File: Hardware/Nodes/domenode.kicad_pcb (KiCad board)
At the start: 2 copper layers, 100 x 70 mm, 86 parts, among them J1 MIC_JUMPER, J10 5V, J11 TOUCH, J12 24V, J13 CAN_BOARD, J15 RGB_SHIELD, J16 RGB_SHIELD, J17 GROVE/I2C, J18 ISP, J19 CAN_IN, J2 MIC_HEADER, J20 CAN_OUT, J21 SWITCHES, J3 SW0, J4 CANTERM, J5 3V3, J6 POWER_TEST, J9 SENSOR, Q1 MMBT918 (2N706 equiv), Q2 MMBT2222A (2N2222 equiv), SW1 SW1, SW2 SW2, SW3 RESET, SW4 BOOT, U1 MINI-360, U2 AMS1117-3.3, U3 ESP32-WROOM, U5 TSDP341xx, U6 SN65HVD230

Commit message: woooo
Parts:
- moved SW1 1.27 mm to (159.8, 136.5)
- moved SW2 1.25 mm to (165.9, 136.5)
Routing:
- net CANGND: track 84.3 -> 113.9 mm, vias 4 -> 6
- net SW1: track 32.4 -> 17.9 mm
- net SW2: track 31.0 -> 29.3 mm

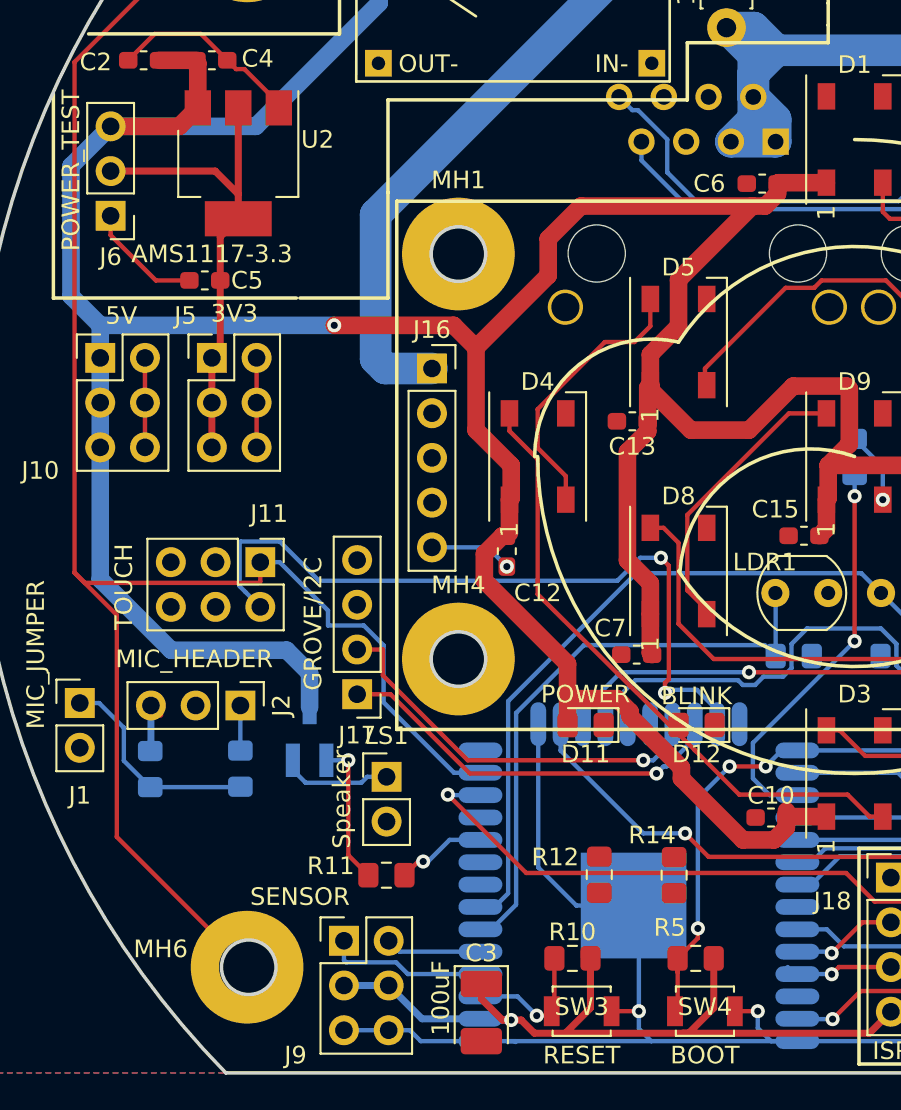
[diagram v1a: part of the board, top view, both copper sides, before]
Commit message: Added moar decoupling caps and laid out in PCB
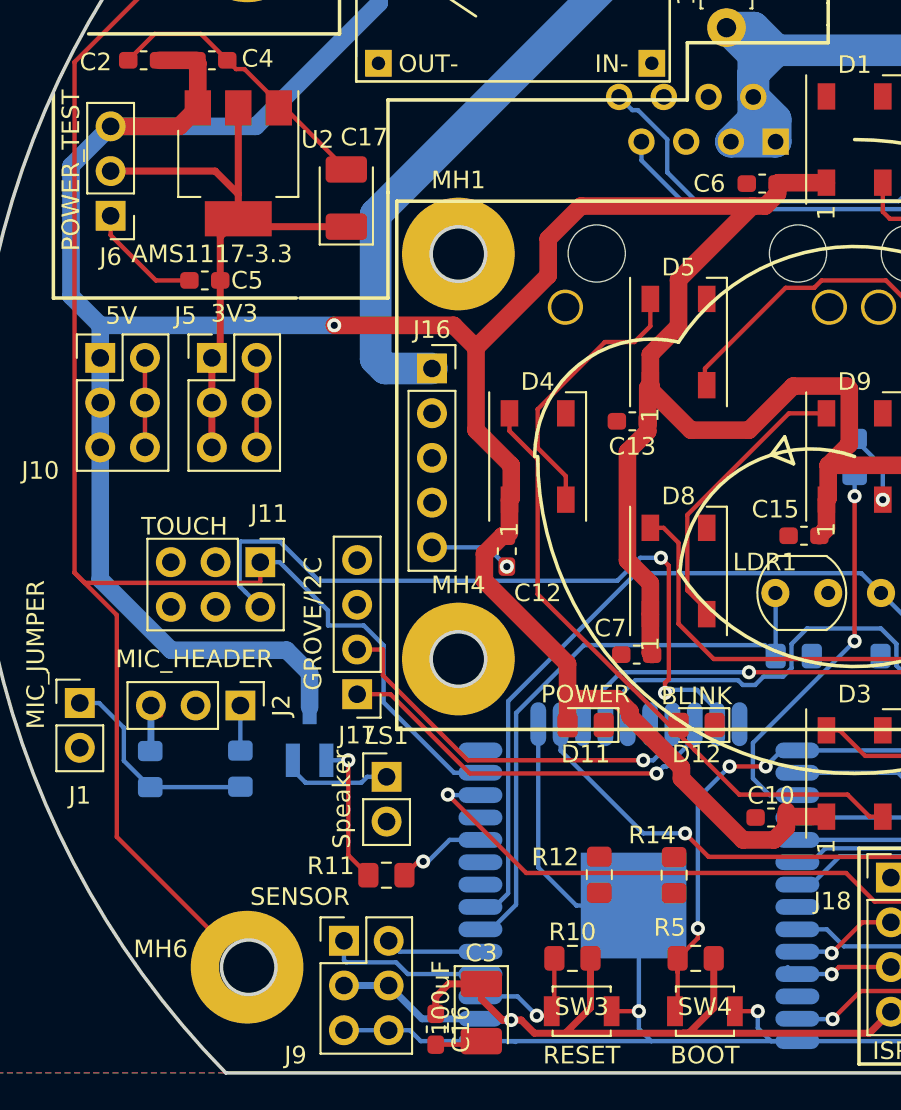
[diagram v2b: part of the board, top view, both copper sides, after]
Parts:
- added C16: 10uF, Capacitor_SMD:C_0603_1608Metric_Pad1.05x0.95mm_HandSolder, F.Cu at (124.7, 137.5)
- added C17: 100uF, Capacitor_Tantalum_SMD:CP_EIA-3528-21_Kemet-B_Pad1.50x2.35mm_HandSolder, F.Cu at (119.6, 90.3)
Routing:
- net VCC: track 95.6 -> 105.8 mm
- net CANGND: track 113.9 -> 121.9 mm

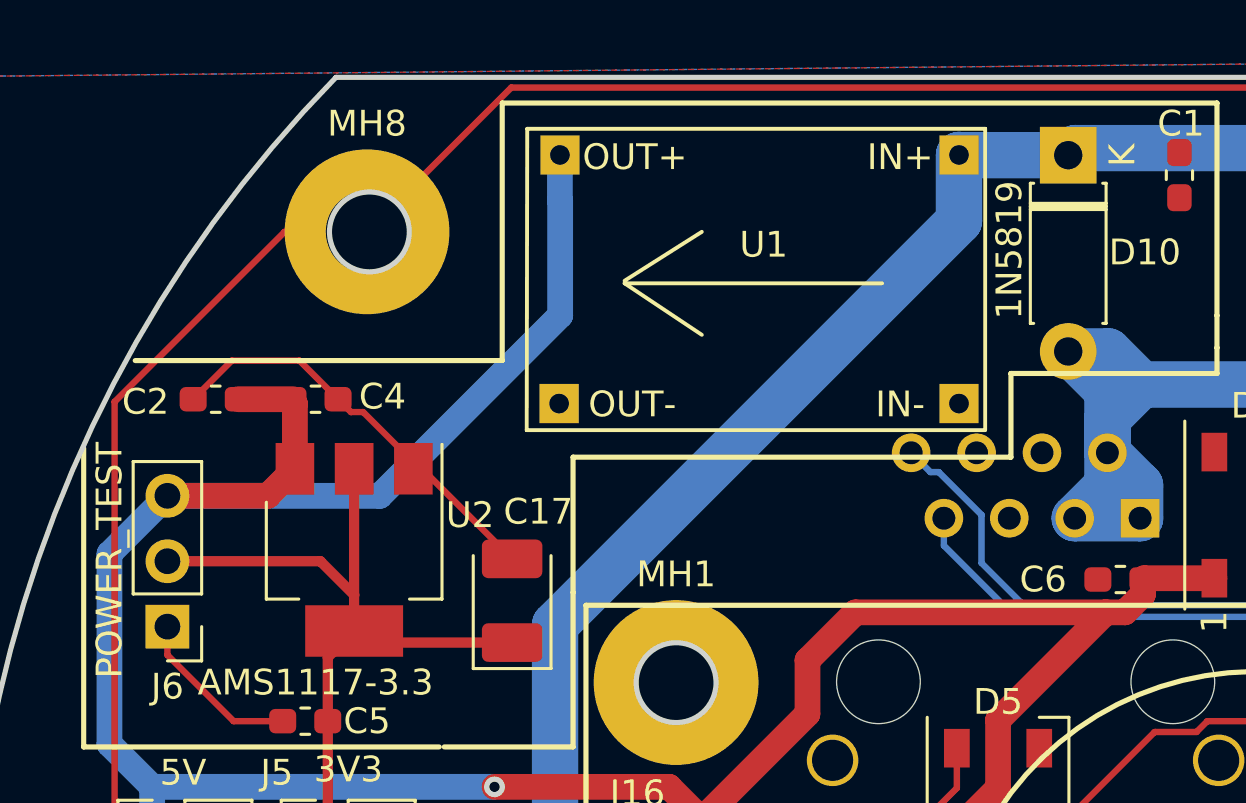
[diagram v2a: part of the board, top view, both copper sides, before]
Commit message: Updated buck regulator footprint to make it easier to solder
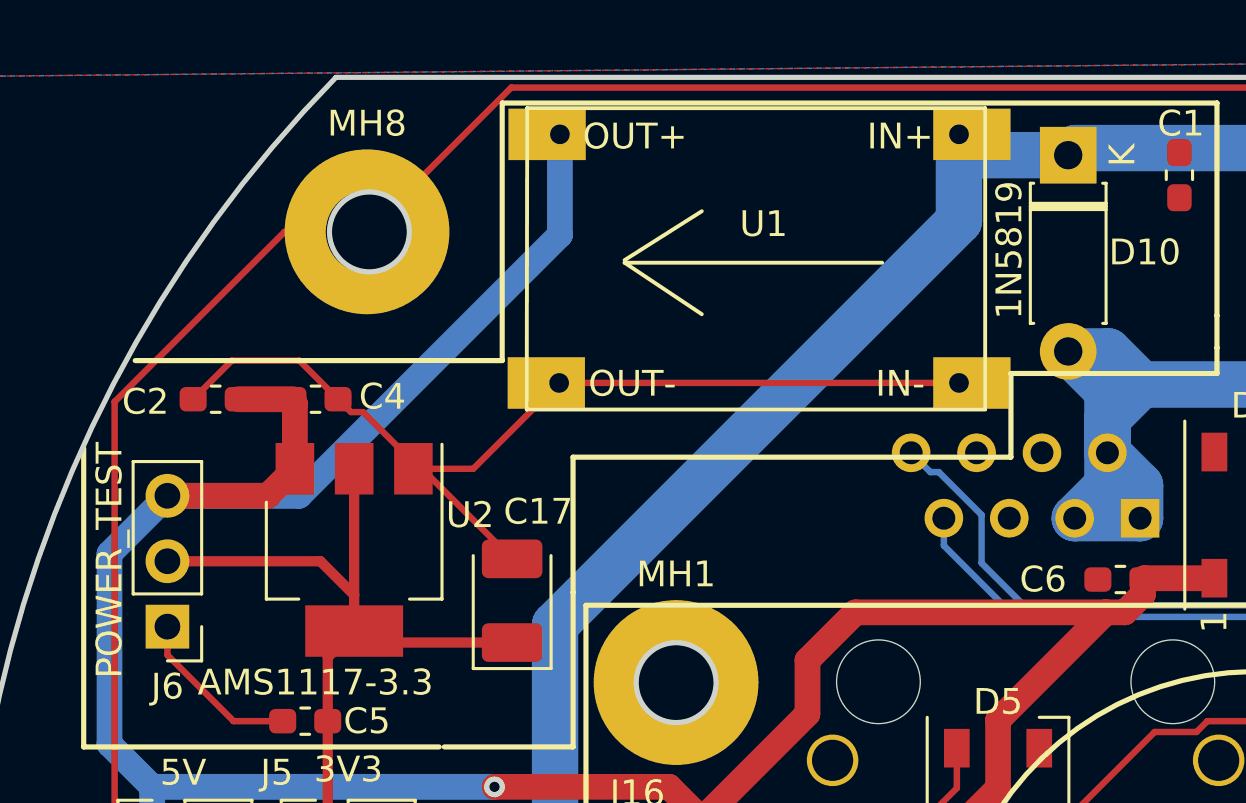
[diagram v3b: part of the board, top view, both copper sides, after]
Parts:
- moved U1 0.80 mm to (138.0, 71.2)
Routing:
- net CANGND: track 121.9 -> 144.4 mm
- net +24V: track 101.8 -> 102.9 mm
- net +5V: track 273.8 -> 272.7 mm

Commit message: Skookum'd C1
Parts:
- C1: footprint Capacitor_SMD:C_0603_1608Metric_Pad1.05x0.95mm_HandSolder -> Capacitor_SMD:C_1210_3225Metric_Pad1.42x2.65mm_HandSolder
- moved D12 7.20 mm to (134.6, 125.5), turned to 270 degrees
- moved D11 6.57 mm to (137.2, 125.5), turned to 90 degrees
- moved R14 3.69 mm to (134.6, 129.3)
- moved R12 3.27 mm to (137.2, 129.4)
- moved C1 2.92 mm to (145.2, 76.7)
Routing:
- net CANGND: track 144.4 -> 195.7 mm, vias 6 -> 11
- net BLINK: track 0.00 -> 14.1 mm, vias 0 -> 1
- net VCC: track 105.8 -> 116.8 mm, vias 2 -> 3
- net +24V: track 102.9 -> 108.9 mm
- net Net-(R17-Pad1): track 0.00 -> 3.31 mm
- net +5V: track 272.7 -> 275.0 mm
- net Net-(D11-Pad1): track 0.00 -> 1.88 mm
- net Net-(D12-Pad2): track 0.00 -> 1.78 mm

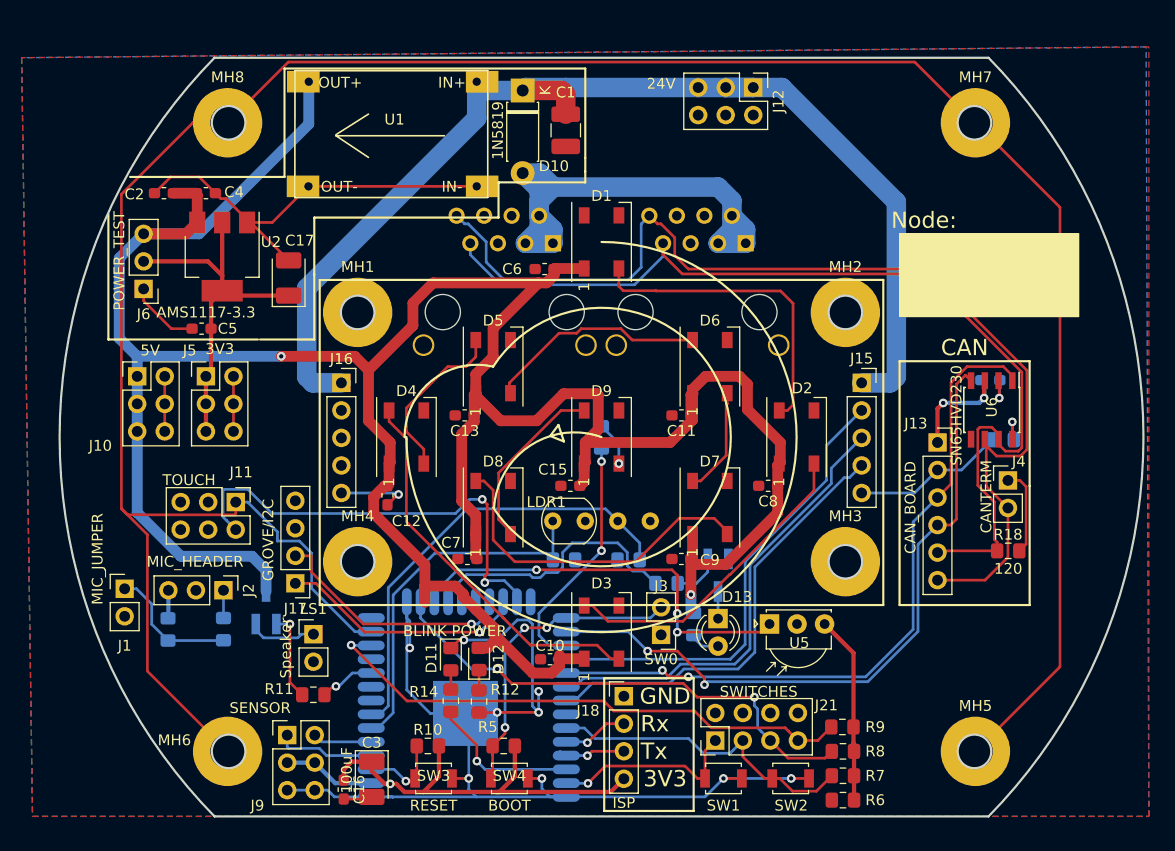
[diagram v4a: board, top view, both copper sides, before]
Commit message: Added 5v rail to rgb header
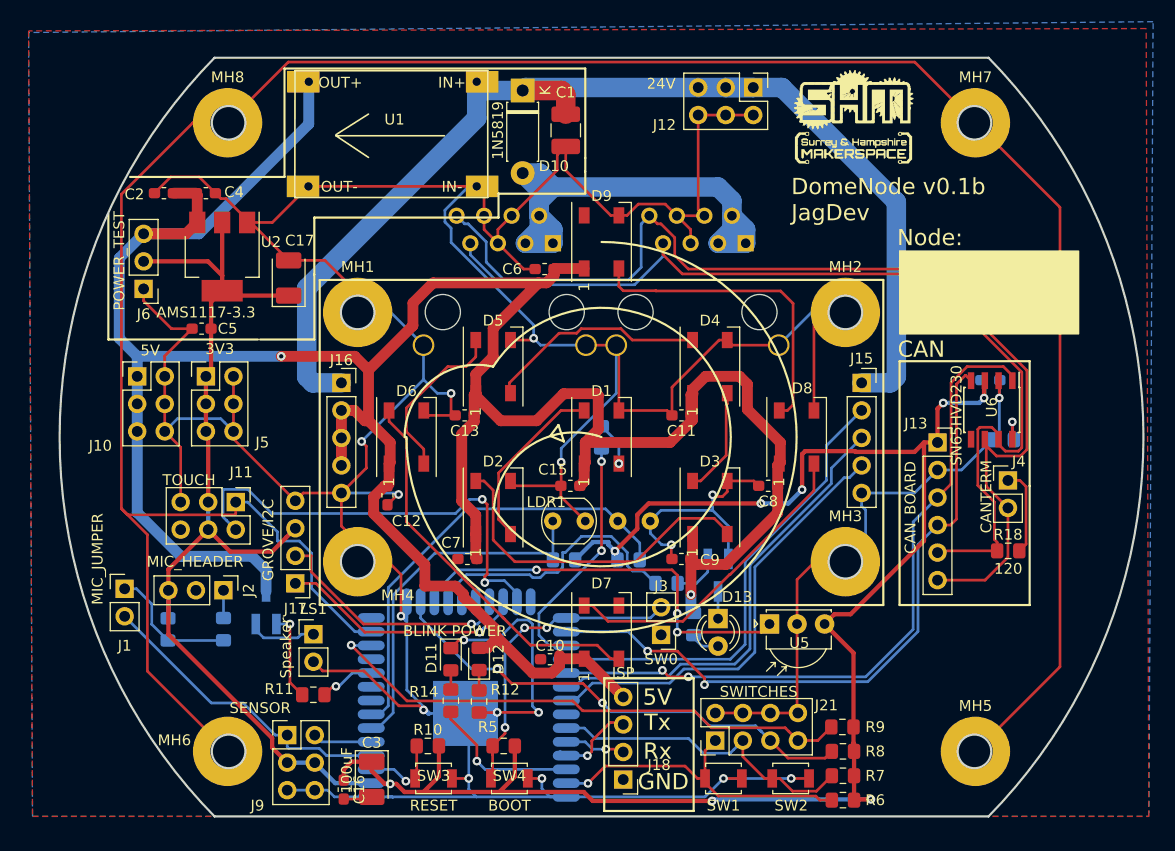
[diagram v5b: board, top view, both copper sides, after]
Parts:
- added shm_logo_small: , shm_logo:shm_logo_small, F.Cu at (165.7, 70.9)
- moved J18 7.69 mm to (150.5, 136.6), turned to 180 degrees
- renumbered D9 to D1, D8 to D2, D7 to D3, D6 to D4, D4 to D6, D3 to D7, D2 to D8, D1 to D9
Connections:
- J16 pad 2: RED -> +5V
- J16 pad 3: GREEN -> +5V
- J16 pad 4: BLUE -> +5V
- J18 pad 4: VCC -> +5V
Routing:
- net CANGND: track 195.7 -> 510.3 mm, vias 11 -> 17
- net VCC: track 116.8 -> 251.2 mm, vias 3 -> 8
- net VP: track 9.18 -> 28.7 mm
- net SW1: track 17.9 -> 30.7 mm
- net +5V: track 275.0 -> 286.5 mm
- net TX: track 6.05 -> 7.65 mm
- net SW3: track 46.5 -> 45.5 mm
- net RX: track 6.07 -> 5.56 mm
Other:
- board text added: "5V"
- board text added: "DomeNode v0.1b JagDev"
- board text removed: "3V3"
